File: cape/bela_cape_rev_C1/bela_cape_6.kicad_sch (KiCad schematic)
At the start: 47 parts, among them IC3 ES9080Q, J12 Conn_01x03, J13 Conn_01x03, J14 Conn_01x03, J15 Conn_01x03, U1 TL974, U2 TL974

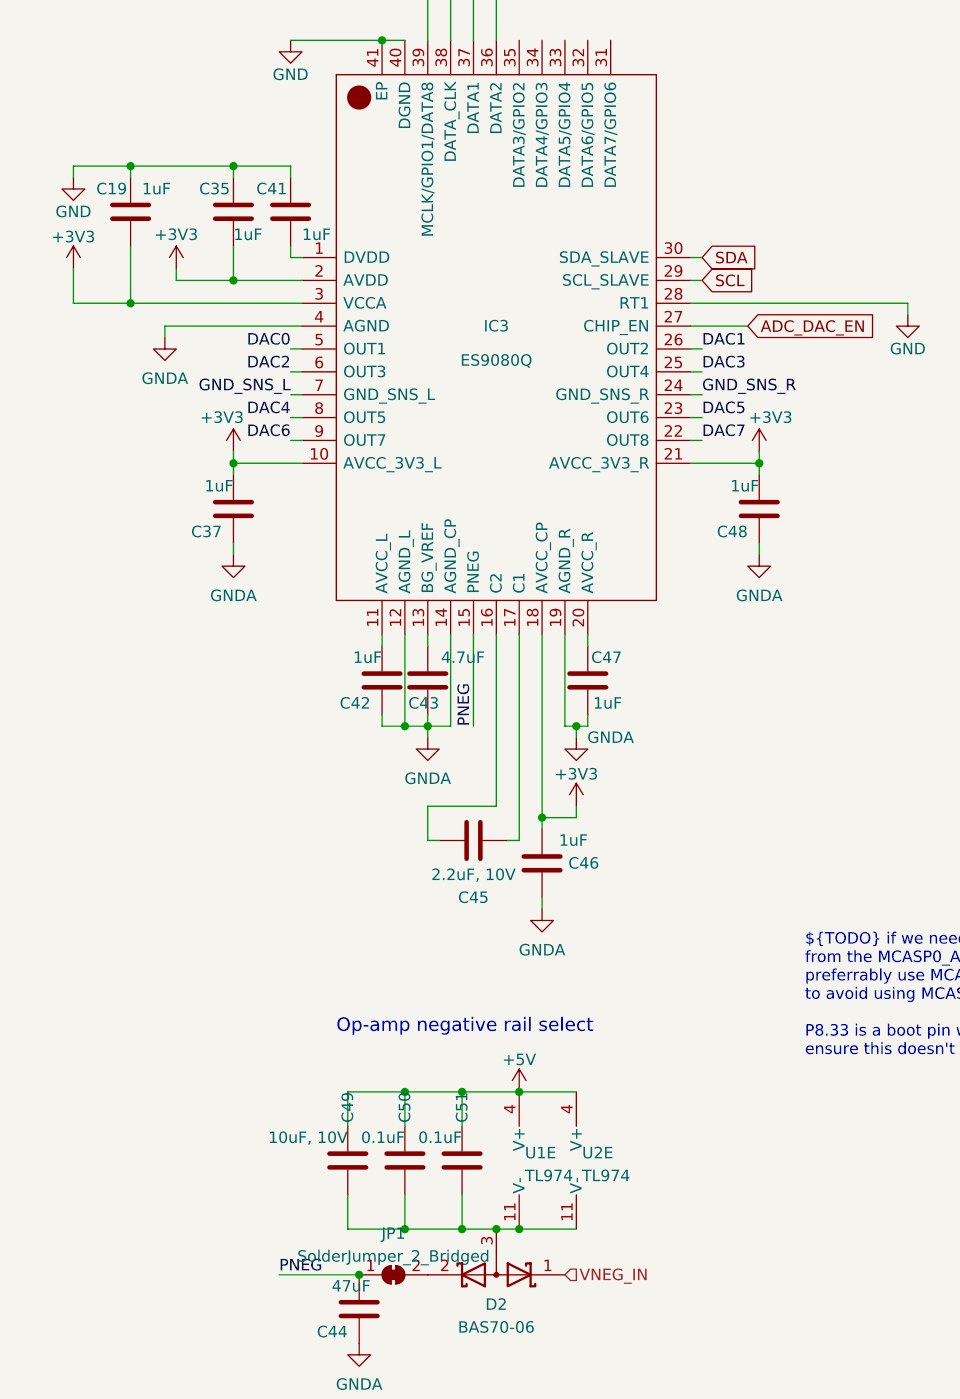
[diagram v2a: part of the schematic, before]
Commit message: Further routing on C1 cape
(cherry picked from commit 232a25b01e013bf194cdc3a343766aa7b43870aa)
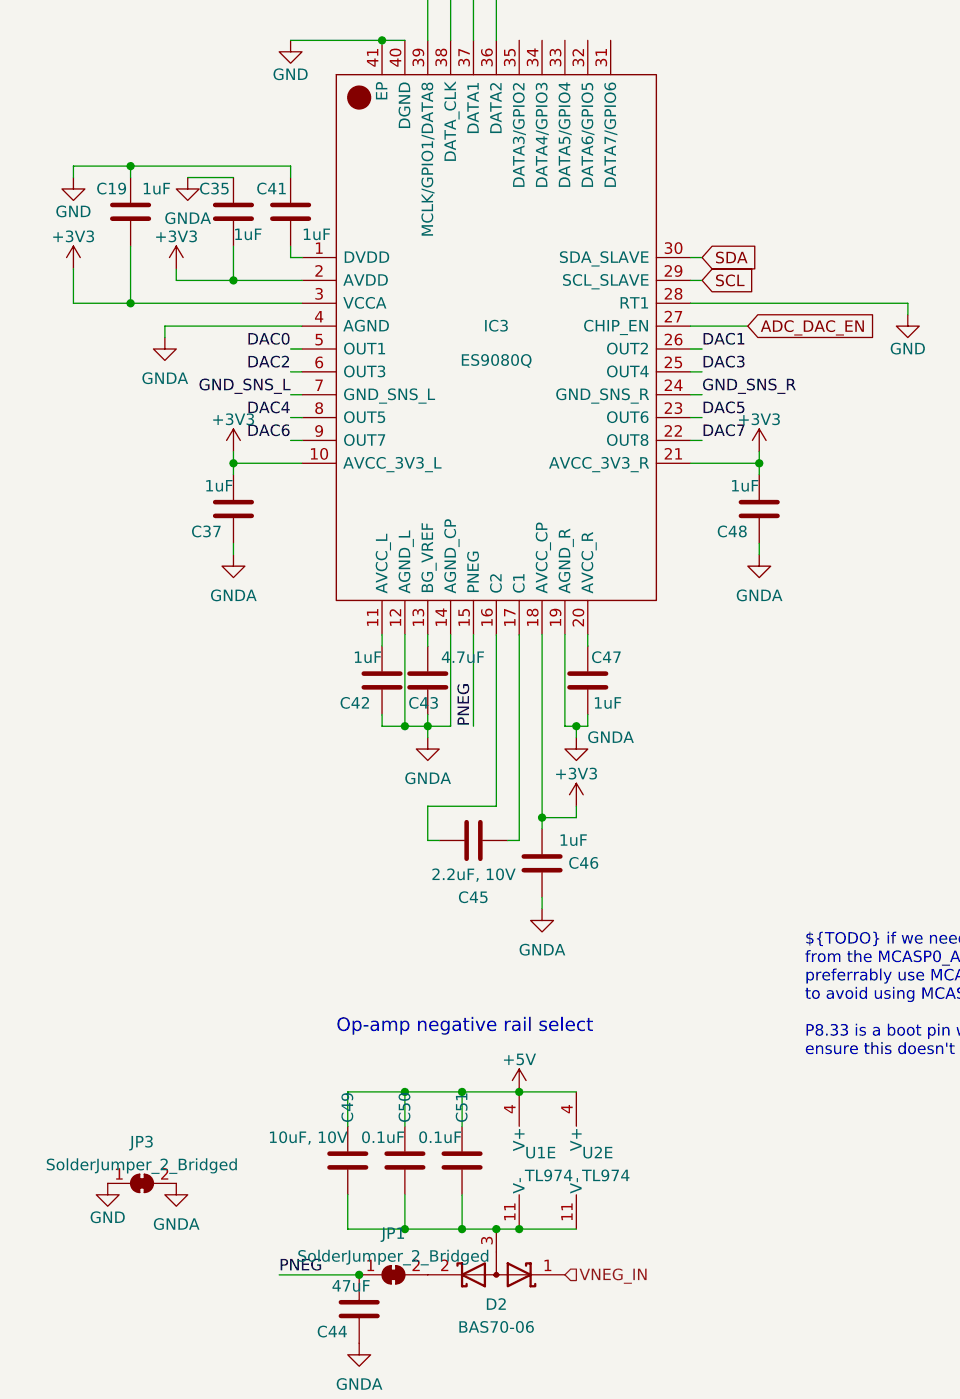
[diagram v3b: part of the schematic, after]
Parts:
- added JP3: SolderJumper_2_Bridged, Jumper:SolderJumper-2_P1.3mm_Bridged_Pad1.0x1.5mm, symbol Jumper:SolderJumper_2_Bridged
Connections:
- net GND: now also JP3.1 (A); no longer C35.1
- net GNDA: now also C35.1, JP3.2 (B)
- net +3.3V renamed +3V3
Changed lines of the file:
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@@
   (junction (at 198.12 66.04) (diameter 0) (color 0 0 0 0)
   )
-  (junction (at 44.45 52.07) (diameter 0) (color 0 0 0 0)
-  )
   (junction (at 149.86 40.64) (diameter 0) (color 0 0 0 0)
   )
@@
     (stroke (width 0) (type default) (color 0 0 0 0))
   )
-  (wire (pts (xy 44.45 52.07) (xy 44.45 53.34))
+  (wire (pts (xy 39.37 53.34) (xy 44.45 53.34))
     (stroke (width 0) (type default) (color 0 0 0 0))
   )
@@
     (stroke (width 0) (type default) (color 0 0 0 0))
   )
-  (wire (pts (xy 33.02 52.07) (xy 44.45 52.07))
+  (wire (pts (xy 33.02 52.07) (xy 50.8 52.07))
     (stroke (width 0) (type default) (color 0 0 0 0))
   )
@@
   )
   (wire (pts (xy 143.51 40.64) (xy 146.05 40.64))
-    (stroke (width 0) (type default) (color 0 0 0 0))
-  )
-  (wire (pts (xy 44.45 52.07) (xy 50.8 52.07))
     (stroke (width 0) (type default) (color 0 0 0 0))
   )
@@
     (pin "3")
   )
+  (symbol (lib_id "power:GNDA") (at 38.1 165.1 0) (unit 1)
+    (in_bom yes) (on_board yes)
+    (property "Reference" "#PWR0165" (id 0) (at 38.1 171.45 0)
+      (effects (font (size 1.27 1.27)) hide)
+    )
+    (property "Value" "GNDA" (id 1) (at 38.1 169.6625 0))
+    (property "Footprint" "" (id 2) (at 38.1 165.1 0)
+      (effects (font (size 1.27 1.27)) hide)
+    )
+    (property "Datasheet" "" (id 3) (at 38.1 165.1 0)
+      (effects (font (size 1.27 1.27)) hide)
+    )
+    (pin "1")
+  )
   (symbol (lib_id "Device:C") (at 194.31 69.85 270) (unit 1)
     (in_bom yes) (on_board yes)
@@
     )
     (property "Datasheet" "" (id 3) (at 173.99 66.04 0)
+      (effects (font (size 1.27 1.27)) hide)
+    )
+    (pin "1")
+  )
+  (symbol (lib_id "power:+3V3") (at 102.87 83.82 0) (unit 1)
+    (in_bom yes) (on_board yes) (fields_autoplaced)
+    (property "Reference" "#PWR0158" (id 0) (at 102.87 87.63 0)
+      (effects (font (size 1.27 1.27)) hide)
+    )
+    (property "Value" "+3V3" (id 1) (at 102.87 80.2442 0))
+    (property "Footprint" "" (id 2) (at 102.87 83.82 0)
+      (effects (font (size 1.27 1.27)) hide)
+    )
+    (property "Datasheet" "" (id 3) (at 102.87 83.82 0)
       (effects (font (size 1.27 1.27)) hide)
     )
@@
     (pin "4")
   )
+  (symbol (lib_id "power:GNDA") (at 39.37 53.34 0) (unit 1)
+    (in_bom yes) (on_board yes) (fields_autoplaced)
+    (property "Reference" "#PWR?" (id 0) (at 39.37 59.69 0)
+      (effects (font (size 1.27 1.27)) hide)
+    )
+    (property "Value" "GNDA" (id 1) (at 39.37 57.9025 0))
+    (property "Footprint" "" (id 2) (at 39.37 53.34 0)
+      (effects (font (size 1.27 1.27)) hide)
+    )
+    (property "Datasheet" "" (id 3) (at 39.37 53.34 0)
+      (effects (font (size 1.27 1.27)) hide)
+    )
+    (pin "1")
+  )
   (symbol (lib_id "power:GNDA") (at 66.04 115.57 0) (unit 1)
     (in_bom yes) (on_board yes)
@@
     (pin "1")
   )
+  (symbol (lib_id "power:+3V3") (at 82.55 123.19 0) (unit 1)
+    (in_bom yes) (on_board yes) (fields_autoplaced)
+    (property "Reference" "#PWR0160" (id 0) (at 82.55 127 0)
+      (effects (font (size 1.27 1.27)) hide)
+    )
+    (property "Value" "+3V3" (id 1) (at 82.55 119.6142 0))
+    (property "Footprint" "" (id 2) (at 82.55 123.19 0)
+      (effects (font (size 1.27 1.27)) hide)
+    )
+    (property "Datasheet" "" (id 3) (at 82.55 123.19 0)
+      (effects (font (size 1.27 1.27)) hide)
+    )
+    (pin "1")
+  )
   (symbol (lib_id "power:GNDA") (at 134.62 118.11 0) (unit 1)
     (in_bom yes) (on_board yes) (fields_autoplaced)
@@
     (property "Datasheet" "" (id 3) (at 134.62 118.11 0)
       (effects (font (size 1.27 1.27)) hide)
-    )
-    (pin "1")
-  )
-  (symbol (lib_id "power:+3.3V") (at 102.87 83.82 0) (unit 1)
-    (in_bom yes) (on_board yes)
-    (property "Reference" "#PWR053" (id 0) (at 102.87 87.63 0)
-      (effects (font (size 1.27 1.27)) hide)
-    )
-    (property "Value" "+3V3" (id 1) (at 104.14 80.01 0))
-    (property "Footprint" "" (id 2) (at 102.87 83.82 0)
-      (effects (font (size 1.524 1.524)))
-    )
-    (property "Datasheet" "" (id 3) (at 102.87 83.82 0)
-      (effects (font (size 1.524 1.524)))
     )
     (pin "1")
@@
     (pin "1")
   )
-  (symbol (lib_id "power:+3.3V") (at 26.67 63.5 0) (unit 1)
-    (in_bom yes) (on_board yes)
-    (property "Reference" "#PWR042" (id 0) (at 26.67 67.31 0)
-      (effects (font (size 1.27 1.27)) hide)
-    )
-    (property "Value" "+3V3" (id 1) (at 26.67 59.944 0))
-    (property "Footprint" "" (id 2) (at 26.67 63.5 0)
-      (effects (font (size 1.524 1.524)))
-    )
-    (property "Datasheet" "" (id 3) (at 26.67 63.5 0)
-      (effects (font (size 1.524 1.524)))
-    )
-    (pin "1")
-  )
-  (symbol (lib_id "power:+3.3V") (at 38.1 63.5 0) (unit 1)
-    (in_bom yes) (on_board yes)
-    (property "Reference" "#PWR044" (id 0) (at 38.1 67.31 0)
-      (effects (font (size 1.27 1.27)) hide)
-    )
-    (property "Value" "+3V3" (id 1) (at 38.1 59.69 0))
-    (property "Footprint" "" (id 2) (at 38.1 63.5 0)
-      (effects (font (size 1.524 1.524)))
-    )
-    (property "Datasheet" "" (id 3) (at 38.1 63.5 0)
-      (effects (font (size 1.524 1.524)))
-    )
-    (pin "1")
-  )
   (symbol (lib_id "Device:C") (at 193.04 95.25 270) (unit 1)
     (in_bom yes) (on_board yes)
@@
     )
     (property "manf#" "CL10A105KP8NNND" (id 4) (at 193.04 95.25 0)
+      (effects (font (size 1.27 1.27)) hide)
+    )
+    (pin "1")
+    (pin "2")
+  )
+  (symbol (lib_id "Jumper:SolderJumper_2_Bridged") (at 34.29 165.1 0) (unit 1)
+    (in_bom yes) (on_board yes) (fields_autoplaced)
+    (property "Reference" "JP3" (id 0) (at 34.29 160.5112 0))
+    (property "Value" "SolderJumper_2_Bridged" (id 1) (at 34.29 163.0481 0))
+    (property "Footprint" "Jumper:SolderJumper-2_P1.3mm_Bridged_Pad1.0x1.5mm" (id 2) (at 34.29 165.1 0)
+      (effects (font (size 1.27 1.27)) hide)
+    )
+    (property "Datasheet" "~" (id 3) (at 34.29 165.1 0)
       (effects (font (size 1.27 1.27)) hide)
     )
@@
     (pin "1")
     (pin "2")
+  )
+  (symbol (lib_id "power:+3V3") (at 26.67 63.5 0) (unit 1)
+    (in_bom yes) (on_board yes) (fields_autoplaced)
+    (property "Reference" "#PWR0162" (id 0) (at 26.67 67.31 0)
+      (effects (font (size 1.27 1.27)) hide)
+    )
+    (property "Value" "+3V3" (id 1) (at 26.67 59.9242 0))
+    (property "Footprint" "" (id 2) (at 26.67 63.5 0)
+      (effects (font (size 1.27 1.27)) hide)
+    )
+    (property "Datasheet" "" (id 3) (at 26.67 63.5 0)
+      (effects (font (size 1.27 1.27)) hide)
+    )
+    (pin "1")
   )
   (symbol (lib_id "power:GNDA") (at 58.42 182.88 0) (unit 1)
@@
     (pin "2")
   )
+  (symbol (lib_id "power:+3V3") (at 38.1 63.5 0) (unit 1)
+    (in_bom yes) (on_board yes) (fields_autoplaced)
+    (property "Reference" "#PWR0161" (id 0) (at 38.1 67.31 0)
+      (effects (font (size 1.27 1.27)) hide)
+    )
+    (property "Value" "+3V3" (id 1) (at 38.1 59.9242 0))
+    (property "Footprint" "" (id 2) (at 38.1 63.5 0)
+      (effects (font (size 1.27 1.27)) hide)
+    )
+    (property "Datasheet" "" (id 3) (at 38.1 63.5 0)
+      (effects (font (size 1.27 1.27)) hide)
+    )
+    (pin "1")
+  )
   (symbol (lib_id "Device:R") (at 153.67 40.64 90) (unit 1)
     (in_bom yes) (on_board yes) (fields_autoplaced)
@@
     (pin "2")
   )
-  (symbol (lib_id "power:+3.3V") (at 44.45 83.82 0) (unit 1)
-    (in_bom yes) (on_board yes)
-    (property "Reference" "#PWR045" (id 0) (at 44.45 87.63 0)
-      (effects (font (size 1.27 1.27)) hide)
-    )
-    (property "Value" "+3V3" (id 1) (at 43.18 80.01 0))
-    (property "Footprint" "" (id 2) (at 44.45 83.82 0)
-      (effects (font (size 1.524 1.524)))
-    )
-    (property "Datasheet" "" (id 3) (at 44.45 83.82 0)
-      (effects (font (size 1.524 1.524)))
-    )
-    (pin "1")
-  )
   (symbol (lib_id "Device:C") (at 154.94 121.92 270) (unit 1)
     (in_bom yes) (on_board yes)
@@
     (pin "2")
   )
-  (symbol (lib_id "power:+3.3V") (at 82.55 123.19 0) (unit 1)
-    (in_bom yes) (on_board yes)
-    (property "Reference" "#PWR051" (id 0) (at 82.55 127 0)
-      (effects (font (size 1.27 1.27)) hide)
-    )
-    (property "Value" "+3V3" (id 1) (at 82.55 119.634 0))
-    (property "Footprint" "" (id 2) (at 82.55 123.19 0)
-      (effects (font (size 1.524 1.524)))
-    )
-    (property "Datasheet" "" (id 3) (at 82.55 123.19 0)
-      (effects (font (size 1.524 1.524)))
+  (symbol (lib_id "power:GND") (at 30.48 165.1 0) (mirror y) (unit 1)
+    (in_bom yes) (on_board yes)
+    (property "Reference" "#PWR0166" (id 0) (at 30.48 171.45 0)
+      (effects (font (size 1.27 1.27)) hide)
+    )
+    (property "Value" "GND" (id 1) (at 30.48 168.91 0))
+    (property "Footprint" "" (id 2) (at 30.48 165.1 0)
+      (effects (font (size 1.27 1.27)) hide)
+    )
+    (property "Datasheet" "" (id 3) (at 30.48 165.1 0)
+      (effects (font (size 1.27 1.27)) hide)
     )
     (pin "1")
@@
     (pin "2")
   )
+  (symbol (lib_id "power:+3V3") (at 44.45 83.82 0) (unit 1)
+    (in_bom yes) (on_board yes) (fields_autoplaced)
+    (property "Reference" "#PWR0159" (id 0) (at 44.45 87.63 0)
+      (effects (font (size 1.27 1.27)) hide)
+    )
+    (property "Value" "+3V3" (id 1) (at 44.45 80.2442 0))
+    (property "Footprint" "" (id 2) (at 44.45 83.82 0)
+      (effects (font (size 1.27 1.27)) hide)
+    )
+    (property "Datasheet" "" (id 3) (at 44.45 83.82 0)
+      (effects (font (size 1.27 1.27)) hide)
+    )
+    (pin "1")
+  )
 )

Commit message: First complete routing of C1 cape
(cherry picked from commit 8c5092941a0b3ec42f55098733fd0108b2086674)
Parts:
- J12, J13, J14, J15: footprint Connector_Molex:Molex_KK-254_AE-6410-03A_1x03_P2.54mm_Vertical -> Connector_PinHeader_2.54mm:PinHeader_1x03_P2.54mm_Vertical
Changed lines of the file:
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@@
       (effects (font (size 1.27 1.27)) (justify left))
     )
-    (property "Footprint" "Connector_Molex:Molex_KK-254_AE-6410-03A_1x03_P2.54mm_Vertical" (id 2) (at 240.03 77.47 0)
+    (property "Footprint" "Connector_PinHeader_2.54mm:PinHeader_1x03_P2.54mm_Vertical" (id 2) (at 240.03 77.47 0)
       (effects (font (size 1.27 1.27)) hide)
     )
@@
   (symbol (lib_id "power:GNDA") (at 39.37 53.34 0) (unit 1)
     (in_bom yes) (on_board yes) (fields_autoplaced)
-    (property "Reference" "#PWR?" (id 0) (at 39.37 59.69 0)
+    (property "Reference" "#PWR0169" (id 0) (at 39.37 59.69 0)
       (effects (font (size 1.27 1.27)) hide)
     )
@@
       (effects (font (size 1.27 1.27)) (justify left))
     )
-    (property "Footprint" "Connector_Molex:Molex_KK-254_AE-6410-03A_1x03_P2.54mm_Vertical" (id 2) (at 240.03 62.23 0)
+    (property "Footprint" "Connector_PinHeader_2.54mm:PinHeader_1x03_P2.54mm_Vertical" (id 2) (at 240.03 62.23 0)
       (effects (font (size 1.27 1.27)) hide)
     )
@@
       (effects (font (size 1.27 1.27)) (justify left))
     )
-    (property "Footprint" "Connector_Molex:Molex_KK-254_AE-6410-03A_1x03_P2.54mm_Vertical" (id 2) (at 240.03 48.26 0)
+    (property "Footprint" "Connector_PinHeader_2.54mm:PinHeader_1x03_P2.54mm_Vertical" (id 2) (at 240.03 48.26 0)
       (effects (font (size 1.27 1.27)) hide)
     )
@@
       (effects (font (size 1.27 1.27)) (justify left))
     )
-    (property "Footprint" "Connector_Molex:Molex_KK-254_AE-6410-03A_1x03_P2.54mm_Vertical" (id 2) (at 240.03 33.02 0)
-      (effects (font (size 1.27 1.27)) hide)
-    )
+    (property "Footprint" "Connector_PinHeader_2.54mm:PinHeader_1x03_P2.54mm_Vertical" (id 2) (at 240.03 33.02 0)
+      (effects (font (size 1.27 1.27)) hide)
+    )
